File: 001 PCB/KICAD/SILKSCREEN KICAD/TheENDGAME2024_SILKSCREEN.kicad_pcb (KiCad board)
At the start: 2 copper layers, 219 x 96.1 mm, 90 parts, among them SW10 SW_Push, SW11 SW_Push, SW12 SW_Push, SW13 SW_Push, SW14 SW_Push, SW15 SW_Push, SW16 SW_Push, SW17 SW_Push, SW18 SW_Push, SW19 SW_Push, SW2 SW_Push, SW20 SW_Push, SW21 SW_Push, SW22 SW_Push, SW23 SW_Push, SW24 SW_Push, SW25 SW_Push, SW26 SW_Push, SW27 SW_Push, SW28 SW_Push, SW29 SW_Push, SW3 SW_Push, SW30 SW_Push, SW31 SW_Push, SW32 SW_Push, SW33 SW_Push, SW34 SW_Push, SW35 SW_Push, SW36 SW_Push, SW37 SW_Push, SW4 SW_Push, SW5 SW_Push, SW6 SW_Push, SW7 SW_Push, SW8 SW_Push, SW9 SW_Push, U2 RP2040-Zero_stolen_from_Purox

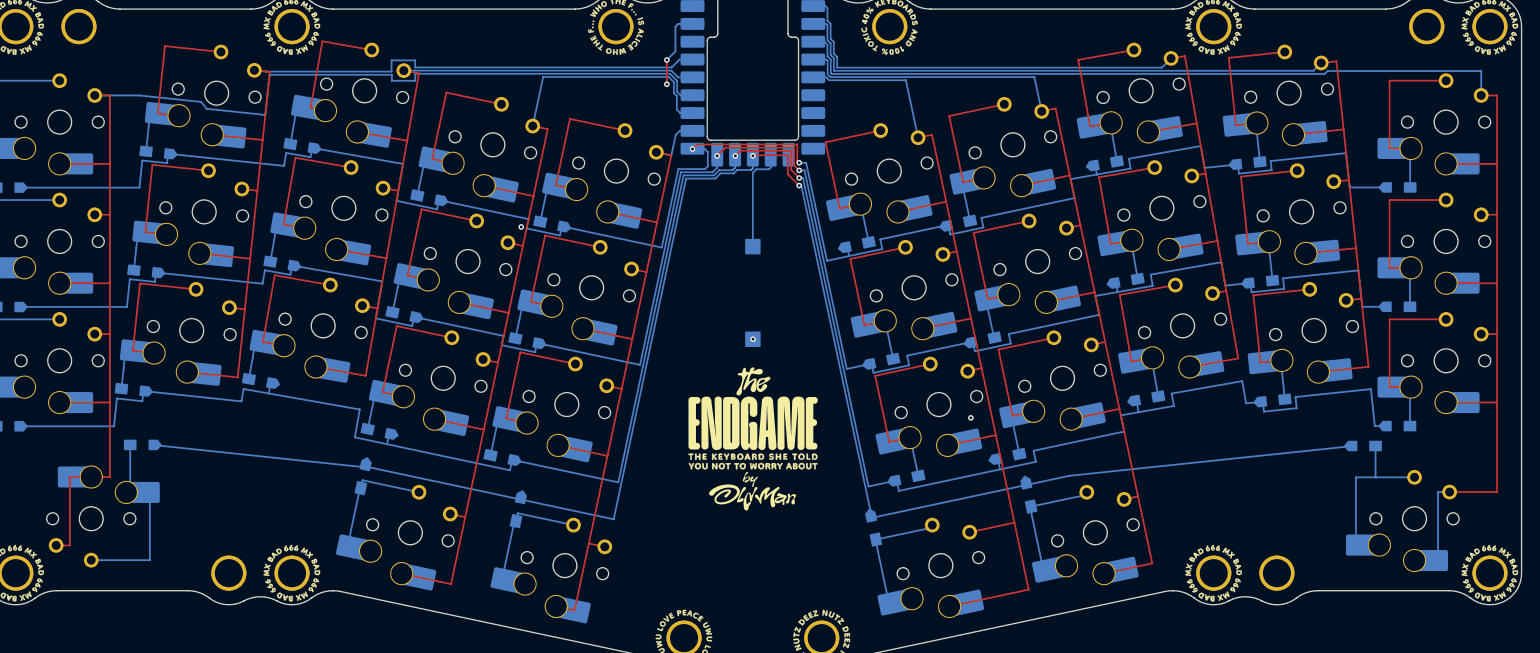
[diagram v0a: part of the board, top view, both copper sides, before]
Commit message: Add Choc V1/V2 hot-swap support and JLCPCB fabrication package
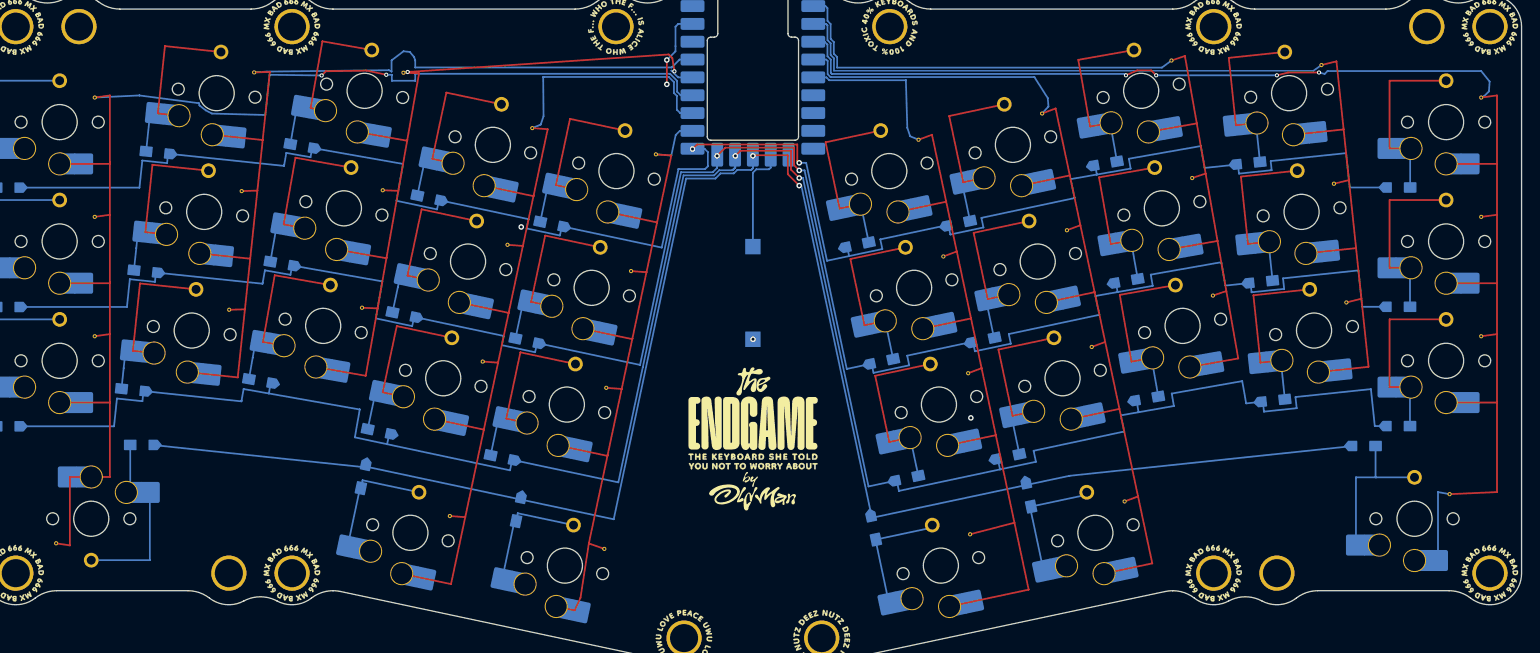
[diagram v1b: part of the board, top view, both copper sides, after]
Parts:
- SW10, SW11, SW12, SW13, SW14, SW15, SW16, SW17, SW18, SW2, SW20, SW21, SW22, SW24, SW25, SW26, SW27, SW28, SW29, SW3, SW30, SW31, SW32, SW33, SW34, SW35, SW36, SW4, SW6, SW7, SW8, SW9: footprint TheEndgame2024:SW_choc_v1_HSxSolder_1u_filets_MBK_blk fixxed flipped solder pads -> TheEndgame2024:SW_choc_v1_v2_HS_1u
- SW19, SW23, SW37, SW5: footprint TheEndgame2024:SW_choc_v1_HSxSolder_1.5u_filets_MBK_blk fixxed flipped solder pads -> TheEndgame2024:SW_choc_v1_v2_HS_1.5u
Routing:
- net col2: track 113.7 -> 116.6 mm, vias 0 -> 2
- net col9: track 206.0 -> 207.9 mm, vias 0 -> 4
- net col1: track 137.6 -> 138.8 mm
- net col6: track 141.1 -> 142.2 mm
- net col3: track 136.6 -> 137.7 mm
- net col5: track 134.6 -> 135.7 mm
- net col0: track 195.0 -> 195.5 mm, vias 0 -> 2
